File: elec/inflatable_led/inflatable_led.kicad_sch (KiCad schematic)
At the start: 24 parts, among them U1 RP2040, U2 W25Q128JVSIQTR, X1 X322512MSB4SI

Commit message: progress on schematic
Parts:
- added BAT1: BH-18650-A5BJ003, footprints:BAT-TH_BH-18650-A5BJ003, symbol local:BH-18650-A5BJ003
- added C15: 220nF, symbol Device:C_Small
- added C16: 4.7uF, symbol Device:C_Small
- added C17, C18, C19: 1uF, symbol Device:C_Small
- added D1: MBR0540T1G, footprints:SOD-123_L2.8-W1.8-LS3.7-RD, symbol local:MBR0540T1G
- added D2, D3, D4, D5, D6, D7: LED, symbol Device:LED
- added L1: 1255AY-100M=P3, footprints:IND-SMD_L6.0-W6.0, symbol local:1255AY-100M=P3
- added LED1, LED2: KT-0603R, footprints:LED0603-RD, symbol local:KT-0603R
- added R6: 0.8R, symbol Device:R_Small
- added R7: 600R, Resistor_SMD:R_0402_1005Metric, symbol Device:R_Small
- added R8, R9: R_Small, symbol Device:R_Small
- added U3: TPS61165DRVR, footprints:WSON-6_L2.0-W2.0-P0.65-TL-EP, symbol local:TPS61165DRVR
- added U4: BQ24040DSQR, footprints:WSON-10_L2.0-W2.0-P0.40-BL-EP, symbol local:BQ24040DSQR
- added USB1: KH-TYPE-C-16P, footprints:USB-C-SMD_KH-TYPE-C-16P, symbol local:KH-TYPE-C-16P
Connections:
- net GND: now also BAT1.1, C15.2, C16.2, C17.2, C18.2, C19.2, R6.2, R7.2, U3.3 (GND), U3.7 (EP), U4.11 (EP), U4.3 (VSS), USB1.1 (EP), USB1.2 (EP), USB1.3 (EP), USB1.4 (EP), USB1.A1 (GND), USB1.A12 (GND), USB1.B1 (GND), USB1.B12 (GND)
- new net: C15.1, U3.2 (COMP)
- new net: D1.2 (A), L1.2, U3.4 (SW)
- new net: C16.1, L1.1, U3.6 (VIN)
- new net: D2.1 (K), D3.2 (A)
- new net: D3.1 (K), D4.2 (A)
- new net: D6.1 (K), D7.2 (A)
- new net: D5.1 (K), D6.2 (A)
- new net: LED1.2 (A), R8.2
- new net: D4.1 (K), D5.2 (A)
- new net: R7.1, U4.2 (ISET)
- new net: LED2.2 (A), R9.2
- new net BAT+: BAT1.2, C19.1, R8.1, R9.1, U4.10 (OUT)
- new net CHARGER_IN: C18.1, U4.1 (IN), U4.7 (ISET2)
- new net CHG_CHG: LED2.1 (K), U4.8 (~{CHG})
- new net CHG_PG: LED1.1 (K), U4.5 (~{PG})
- new net DIM_CTRL: U3.5 (CTRL)
- new net LED_SINK: D7.1 (K), R6.1, U3.1 (FB)
- new net LED_SOURCE: C17.1, D1.1 (K), D2.2 (A)
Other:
- moved on the sheet: BTBOOT0, BTRESET1, C1, C10, C11, C12, C13, C14, C2, C3, C4, C5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

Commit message: checking schematic
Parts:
- removed USB1: KH-TYPE-C-16P, footprints:USB-C-SMD_KH-TYPE-C-16P, symbol local:KH-TYPE-C-16P
- added BTRESET2: TS-1187A-B-A-B, footprints:SW-SMD_4P-L5.1-W5.1-P3.70-LS6.5-TL-2, symbol footprints:TS-1187A-B-A-B
- added C20, C21: 100nF, Capacitor_SMD:C_0805_2012Metric, symbol Device:C_Small
- added C22: 10nF, Capacitor_SMD:C_0402_1005Metric, symbol Device:C_Small
- added D8, D9: MBR0540T1G, footprints:SOD-123_L2.8-W1.8-LS3.7-RD, symbol local:MBR0540T1G
- added J1: Header-Male-2.54_1x20, footprints:HDR-TH_20P-P2.54-V-M-1, symbol footprints:Header-Male-2.54_1x20
- added R10, R11: 5.1K, Resistor_SMD:R_0402_1005Metric, symbol Device:R_Small
- added R12: 100R, Resistor_SMD:R_0402_1005Metric, symbol Device:R_Small
- added R13, R14, R15: 10K, Resistor_SMD:R_0402_1005Metric, symbol Device:R_Small
- added R16: 100R, symbol Device:R_Small
- added TP1, TP2: TestPoint, symbol Connector:TestPoint
- added TP3, TP4, TP5, TPCC1, TPCC2, TP_POWER_OR_1: TestPoint, TestPoint:TestPoint_Pad_D1.5mm, symbol Connector:TestPoint
- added U5: AMS1117-3.3, footprints:SOT-223-3_L6.5-W3.4-P2.30-LS7.0-BR, symbol footprints:AMS1117-3.3
- added U6: F.0603.00026/P2-0603B1TS2-06T-001, footprints:LED0603-RD, symbol footprints:F.0603.00026_P2-0603B1TS2-06T-001
- added U7: SI2323DS, footprints:SOT-23-3_L2.9-W1.3-P1.90-LS2.4-BR, symbol local:SI2323DS
- added USB2: KH-TYPE-C-16P, footprints:USB-C-SMD_KH-TYPE-C-16P, symbol footprints:KH-TYPE-C-16P
- BTBOOT0, BTRESET1: footprint local:SW-SMD_4P-L5.1-W5.1-P3.70-LS6.5-TL-2 -> footprints:SW-SMD_4P-L5.1-W5.1-P3.70-LS6.5-TL-2
- C3: footprint (none) -> Mounting_Wuerth:Mounting_Wuerth_WA-SMSI-M2_H4mm_9774040243
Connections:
- net +1V0: now also U1.45 (VREG_VOUT)
- net +3.3V: now also C21.1, R15.1, U5.2 (VOUT), U5.4 (VOUT), U6.2 (A)
- net +3V3: now also U1.44 (VREG_IN)
- net DIM_CTRL: now also U1.6 (GPIO4)
- net GND: now also BTRESET2.3 (C), BTRESET2.4 (D), C20.2, C21.2, C22.2, R10.2, R11.2, R12.2, R14.2, U5.1 (GND), USB2.1 (EP), USB2.2 (EP), USB2.3 (EP), USB2.4 (EP), USB2.A1 (GND), USB2.A12 (GND), USB2.B1 (GND), USB2.B12 (GND)
- net LED_IN: now reaches C16.1, L1.1, U3.6 (VIN)
- net LED_IN: now also TP2.1, U7.3 (D)
- net at U1.12 (GPIO9): now also J1.1
- net at U1.13 (GPIO10): now also J1.2
- net at U1.14 (GPIO11): now also J1.3
- net at U1.15 (GPIO12): now also J1.4
- net at U1.16 (GPIO13): now also J1.5
- net at U1.17 (GPIO14): now also J1.6
- net at U1.18 (GPIO15): now also J1.7
- net SWCLK: now reaches U1.24 (SWCLK)
- net SWCLK: now also TP4.1
- net SWD: now reaches U1.25 (SWD)
- net SWD: now also TP5.1
- net at U1.27 (GPIO16): now also J1.8
- net at U1.28 (GPIO17): now also J1.9
- net at U1.29 (GPIO18): now also J1.10
- net at U1.30 (GPIO19): now also J1.11
- net at U1.31 (GPIO20): now also J1.12
- net at U1.32 (GPIO21): now also J1.13
- net at U1.34 (GPIO22): now also J1.14
- net at U1.35 (GPIO23): now also J1.15
- net at U1.36 (GPIO24): now also J1.16
- net at U1.37 (GPIO25): now also J1.17
- net BAT_SENSE: now reaches U1.38 (GPIO26_ADC0)
- net BAT_SENSE: now also R13.2, R14.1, TP3.1
- net at U1.39 (GPIO27_ADC1): now also J1.18
- net at U1.40 (GPIO28_ADC2): now also J1.19
- net at U1.41 (GPIO29_ADC3): now also J1.20
- net LED_ON: now reaches U1.5 (GPIO3)
- net LED_ON: now also R16.2
- net BAT+ renamed +BATT
- net +BATT: now also D8.2 (A), R13.1, U7.2 (S)
- net CHARGER_IN renamed VBUS
- net VBUS: now also D9.2 (A), USB2.A4 (VBUS), USB2.A9 (VBUS), USB2.B4 (VBUS), USB2.B9 (VBUS)
- net usb_dm renamed USB_DM
- net USB_DM: now also USB2.A7 (DN1), USB2.B7 (DN2)
- net usb_dp renamed USB_DP
- net USB_DP: now also USB2.A6 (DP1), USB2.B6 (DP2)
- new net: R12.1, U6.1 (K)
- new net: R16.1, TP1.1, U7.1 (G)
- new net ON_OFF_BT: BTRESET2.1 (A), BTRESET2.2 (B), C22.1, R15.2
- new net POWER_IN_OR: C20.1, D8.1 (K), D9.1 (K), TP_POWER_OR_1.1, U5.3 (VIN)
- new net USB_CC1: R10.1, TPCC1.1, USB2.A5 (CC1)
- new net USB_CC2: R11.1, TPCC2.1, USB2.B5 (CC2)
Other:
- note added: "0.2 V [VREF] / 0.25 A = 0.8R"
- note added: "BATTERY"
- note added: "BATTERY SENSE"
- note added: "CHARGER"
- note added: "LDO POWER SUPPLY"
- note added: "LED ARE ONLY BEING POWERED FROM BATTERY, NOT USB"
- note added: "LED DRIVER"
- note added: "LED STRING"
- note added: "LED SWITCH"
- note added: "MICRO"
- note added: "POWER OR"
- note added: "UI"
- note added: "USB"
- moved on the sheet: C18, D2, D3, D4, D5, D6, D7

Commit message: layout almost done + CI
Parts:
- removed BTRESET2: TS-1187A-B-A-B, footprints:SW-SMD_4P-L5.1-W5.1-P3.70-LS6.5-TL-2, symbol footprints:TS-1187A-B-A-B
- added BAT2: BH-18650-A5BJ003, footprints:BAT-TH_BH-18650-A5BJ003, symbol local:BH-18650-A5BJ003
- added D10, D11, D12, D13, D14, D15: LED, footprints:GW JTLPS1EM, symbol Device:LED
- added H1, H2, H3, H4: MountingHole, MountingHole:MountingHole_3.2mm_M3_Pad_Via, symbol Mechanical:MountingHole
- added J2, J3: Conn_01x02_Pin, Connector_PinHeader_2.54mm:PinHeader_1x02_P2.54mm_Vertical, symbol Connector:Conn_01x02_Pin
- added SW1: TS-1093C-A7B2-D1, footprints:SW-TH_TS-1093C-A7B3-D1, symbol local:TS-1093C-A7B2-D1
- added TP6, TP_DIM_CTRL_1: TestPoint, TestPoint:TestPoint_Pad_D1.5mm, symbol Connector:TestPoint
- C1, C10, C11, C2, C4, C5, C6, C7, C9: footprint (none) -> Capacitor_SMD:C_0402_1005Metric
- C12, C16, C17, C18, C19, C8: footprint (none) -> Capacitor_SMD:C_0805_2012Metric
- C15: footprint (none) -> Capacitor_SMD:C_0603_1608Metric
- C3: footprint Mounting_Wuerth:Mounting_Wuerth_WA-SMSI-M2_H4mm_9774040243 -> Capacitor_SMD:C_0402_1005Metric
- D2: footprint (none) -> footprints:GW JTLPS1EM; LCSC Part (none) -> C5220764
- D3, D4, D5, D6, D7: footprint (none) -> footprints:GW JTLPS1EM
- J1: now not fitted
- R1, R16, R2, R3: footprint (none) -> Resistor_SMD:R_0402_1005Metric
- R6: footprint (none) -> Resistor_SMD:R_0805_2012Metric_Pad1.20x1.40mm_HandSolder
- R8, R9: value R_Small -> 100R; footprint (none) -> Resistor_SMD:R_0402_1005Metric
- TP_LED_ON1: renamed from TP1; footprint (none) -> TestPoint:TestPoint_Pad_D1.5mm
- TP_SW_LED1: renamed from TP2; footprint (none) -> TestPoint:TestPoint_Pad_D1.5mm
- renumbered LED2 to LED_CHG_2, LED1 to LED_PG_1
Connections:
- net qspi_ss is gone; now on net QSPI_SS: BTBOOT0.1 (A), BTBOOT0.2 (B), C14.1, R5.2
- net +3.3V: now also C3.1, C4.1, C5.1, C6.1, C7.1, C8.1, U1.1 (IOVDD), U1.10 (IOVDD), U1.22 (IOVDD), U1.33 (IOVDD), U1.42 (IOVDD), U1.43 (ADC_AVDD), U1.44 (VREG_IN), U1.48 (USB_VDD), U1.49 (IOVDD), J3.2 (Pin_2)
- net +3V3: no longer C3.1, C4.1, C5.1, C6.1, C7.1, C8.1, U1.1 (IOVDD), U1.10 (IOVDD), U1.22 (IOVDD), U1.33 (IOVDD), U1.42 (IOVDD), U1.43 (ADC_AVDD), U1.44 (VREG_IN), U1.49 (IOVDD)
- net +BATT: now also BAT2.2, TP6.1
- net BAT_SENSE: now also U1.41 (GPIO29_ADC3); no longer U1.38 (GPIO26_ADC0)
- net DIM_CTRL: now also TP_DIM_CTRL_1.1
- net GND: now also BAT2.1, J3.1 (Pin_1), SW1.2, SW1.3 (EP), SW1.4 (EP)
- net LED_SINK: now also D15.1 (K), J2.2 (Pin_2)
- net LED_SOURCE: now also D10.2 (A), J2.1 (Pin_1)
- net ON_OFF_BT: now also U1.7 (GPIO5), SW1.1
- net at J1.18: now also U1.38 (GPIO26_ADC0); no longer U1.39 (GPIO27_ADC1)
- net at J1.19: now also U1.39 (GPIO27_ADC1); no longer U1.40 (GPIO28_ADC2)
- net at J1.20: now also U1.40 (GPIO28_ADC2); no longer U1.41 (GPIO29_ADC3)
- new net: D12.1 (K), D13.2 (A)
- new net: D11.1 (K), D12.2 (A)
- new net: D10.1 (K), D11.2 (A)
- new net: D14.1 (K), D15.2 (A)
- new net: D13.1 (K), D14.2 (A)

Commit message: add all part numbers
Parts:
- C1, C2: LCSC Part (none) -> C1554
- C10, C11, C3, C4, C5, C6, C7, C9: LCSC Part (none) -> C49678
- C12, C17, C18, C19, C8: LCSC Part (none) -> C28323
- C13, C14, C22: LCSC Part (none) -> C15195
- C15: LCSC Part (none) -> C16772
- C16: LCSC Part (none) -> C23733
- J2, J3: now not fitted
- R1: LCSC Part (none) -> C11702
- R10, R11: LCSC Part (none) -> C25905
- R12, R16, R8, R9: LCSC Part (none) -> C25076
- R13, R14: value 10K -> 100K; LCSC Part (none) -> C25741
- R15, R4, R5: LCSC Part (none) -> C25744
- R2, R3: LCSC Part (none) -> C25100
- R6: LCSC Part (none) -> C175720

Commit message: fix footprint + add pn
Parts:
- C20, C21: footprint Capacitor_SMD:C_0805_2012Metric -> Capacitor_SMD:C_0402_1005Metric
- R7: LCSC Part (none) -> C2076855
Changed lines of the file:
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@@
 			)
 		)
-		(property "Footprint" "Capacitor_SMD:C_0805_2012Metric"
+		(property "Footprint" "Capacitor_SMD:C_0402_1005Metric"
 			(at 447.04 147.32 0)
 			(effects
@@
 			)
 		)
-		(property "Footprint" "Capacitor_SMD:C_0805_2012Metric"
+		(property "Footprint" "Capacitor_SMD:C_0402_1005Metric"
 			(at 433.07 147.32 0)
 			(effects
@@
 			(at 240.03 130.81 0)
 			(effects
+				(font
+					(size 1.27 1.27)
+				)
+				(hide yes)
+			)
+		)
+		(property "LCSC Part" "C2076855"
+			(at 240.03 130.81 0)
+			(effects

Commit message: fix more footprints
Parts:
- C10, C11, C20, C21, C3, C4, C5, C6, C7, C9: LCSC Part C49678 -> C1525
- C15: footprint Capacitor_SMD:C_0603_1608Metric -> Capacitor_SMD:C_0402_1005Metric
- C16: footprint Capacitor_SMD:C_0805_2012Metric -> Capacitor_SMD:C_0402_1005Metric
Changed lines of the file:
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@@
 			)
 		)
-		(property "LCSC Part" "C49678"
+		(property "LCSC Part" "C1525"
 			(at 27.94 31.75 0)
 			(effects
@@
 			)
 		)
-		(property "LCSC Part" "C49678"
+		(property "LCSC Part" "C1525"
 			(at 59.69 31.75 0)
 			(effects
@@
 			)
 		)
-		(property "LCSC Part" "C49678"
+		(property "LCSC Part" "C1525"
 			(at 447.04 147.32 0)
 			(effects
@@
 			)
 		)
-		(property "Footprint" "Capacitor_SMD:C_0603_1608Metric"
+		(property "Footprint" "Capacitor_SMD:C_0402_1005Metric"
 			(at 241.3 63.5 0)
 			(effects
@@
 			)
 		)
-		(property "Footprint" "Capacitor_SMD:C_0805_2012Metric"
+		(property "Footprint" "Capacitor_SMD:C_0402_1005Metric"
 			(at 228.6 48.26 0)
 			(effects
@@
 			)
 		)
-		(property "LCSC Part" "C49678"
+		(property "LCSC Part" "C1525"
 			(at 69.85 31.75 0)
 			(effects
@@
 			)
 		)
-		(property "LCSC Part" "C49678"
+		(property "LCSC Part" "C1525"
 			(at 38.1 31.75 0)
 			(effects
@@
 			)
 		)
-		(property "LCSC Part" "C49678"
+		(property "LCSC Part" "C1525"
 			(at 49.53 31.75 0)
 			(effects
@@
 			)
 		)
-		(property "LCSC Part" "C49678"
+		(property "LCSC Part" "C1525"
 			(at 107.95 31.75 0)
 			(effects
@@
 			)
 		)
-		(property "LCSC Part" "C49678"
+		(property "LCSC Part" "C1525"
 			(at 119.38 31.75 0)
 			(effects
@@
 			)
 		)
-		(property "LCSC Part" "C49678"
+		(property "LCSC Part" "C1525"
 			(at 97.79 31.75 0)
 			(effects
@@
 			)
 		)
-		(property "LCSC Part" "C49678"
+		(property "LCSC Part" "C1525"
 			(at 433.07 147.32 0)
 			(effects

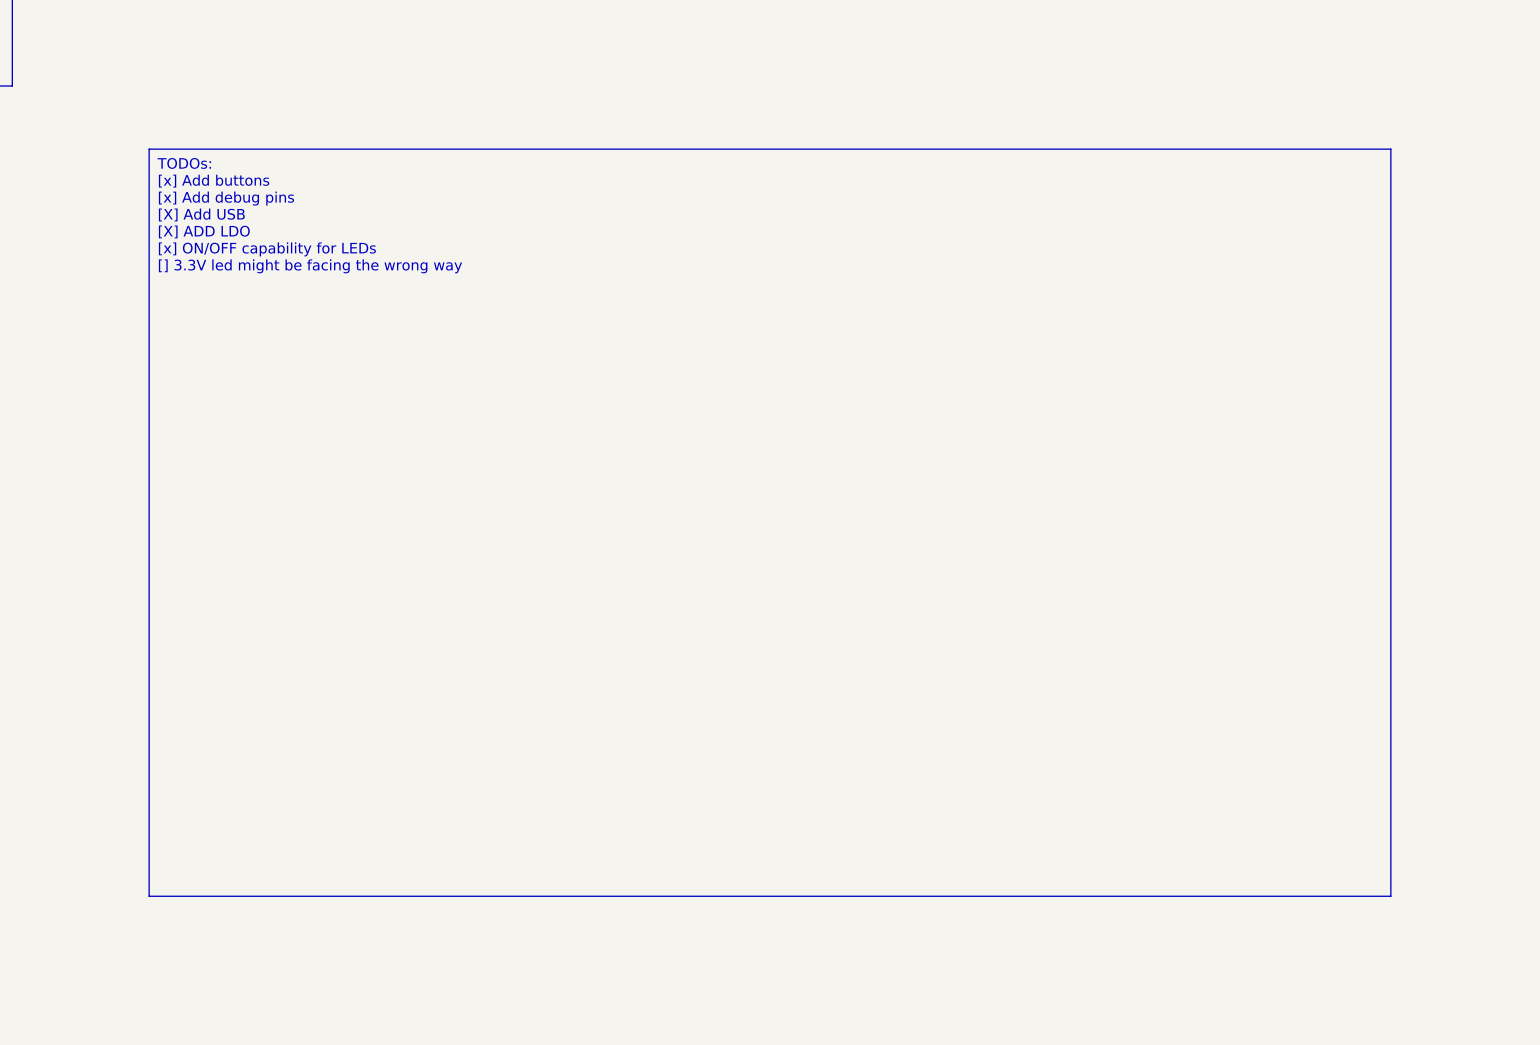
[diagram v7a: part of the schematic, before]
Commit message: leds in the wrong order
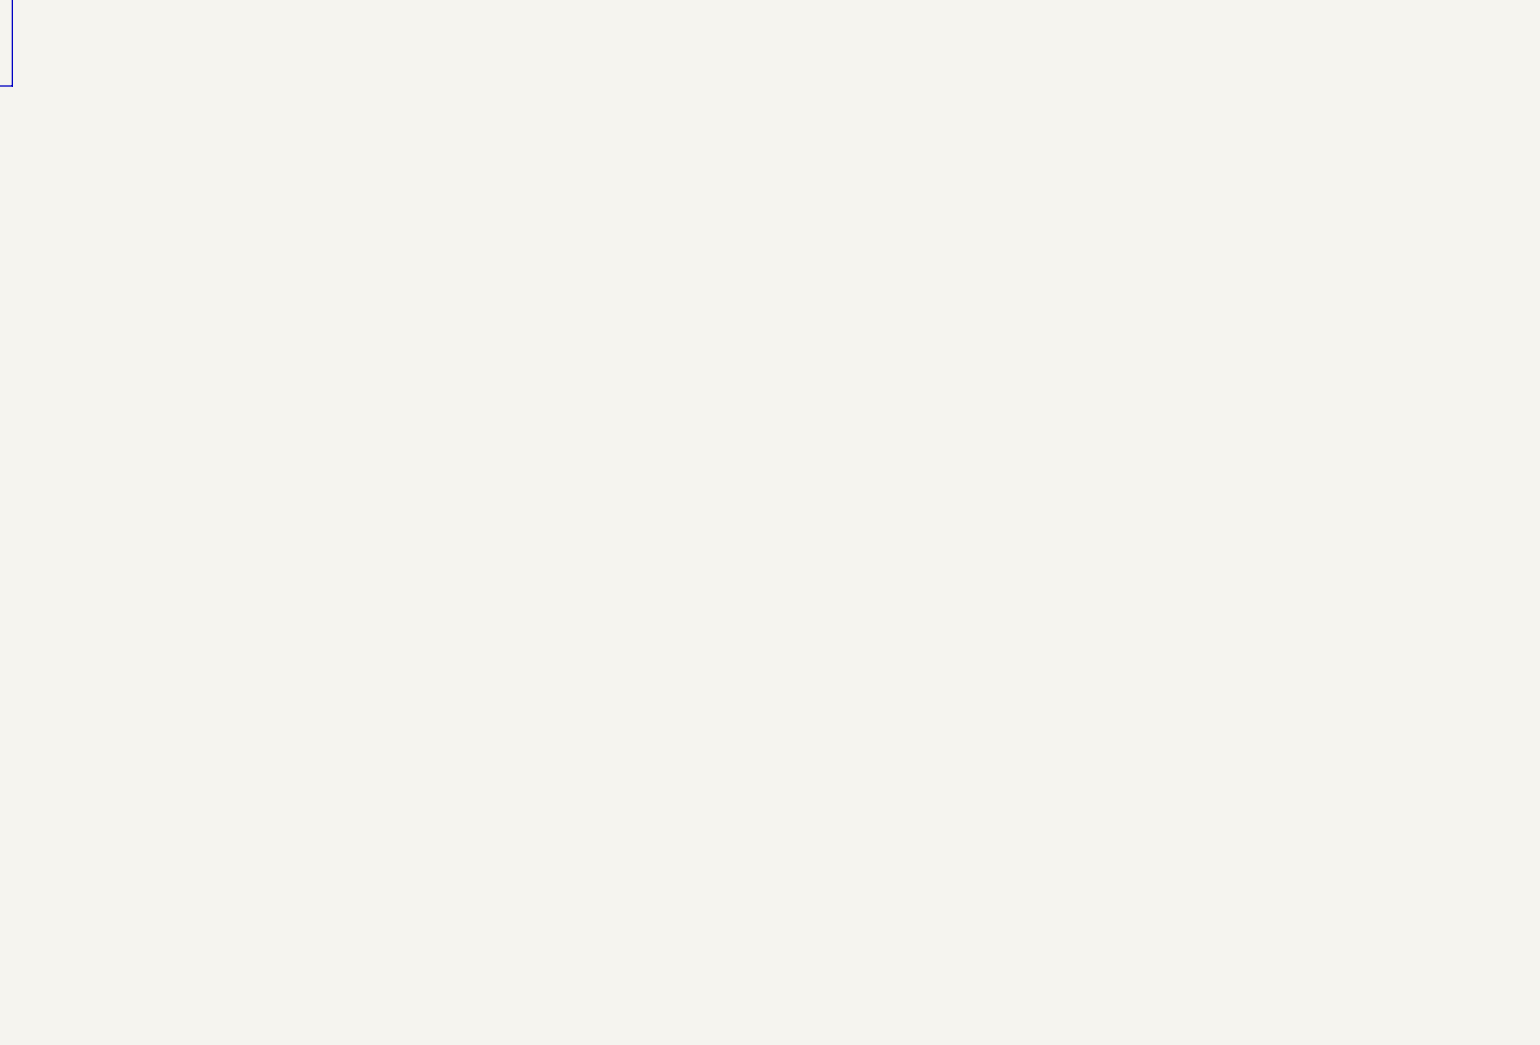
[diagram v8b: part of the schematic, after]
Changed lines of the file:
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@@
-		)
-	)
-	(text_box "TODOs:\n[x] Add buttons\n[x] Add debug pins\n[X] Add USB\n[X] ADD LDO\n[x] ON/OFF capability for LEDs\n[] 3.3V led might be facing the wrong way"
-		(exclude_from_sim no)
-		(at 344.17 241.3 0)
-		(size 149.86 90.17)
-		(stroke
-			(width 0)
-			(type default)
-		)
-		(fill
-			(type none)
-		)
-		(effects
-			(font
-				(size 1.27 1.27)
-			)
-			(justify left top)
 		)
 	)
